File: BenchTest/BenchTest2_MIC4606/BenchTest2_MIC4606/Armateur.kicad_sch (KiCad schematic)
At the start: 15 parts, among them Q1 Q_NMOS_DGS, Q2 Q_NMOS_DGS, U1 TLP2767

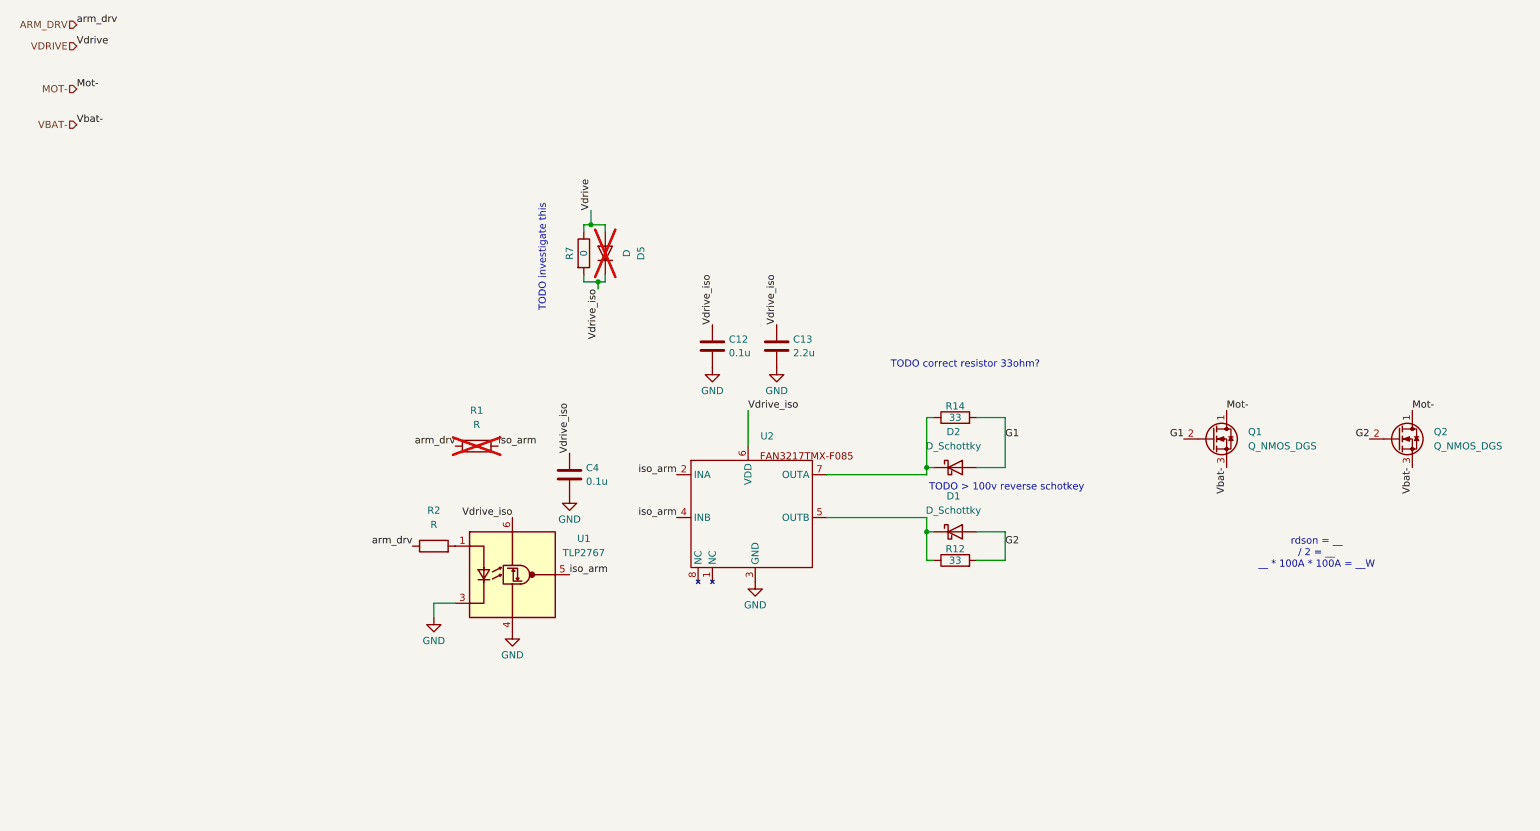
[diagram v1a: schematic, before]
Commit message: Defined Some parts, added notes for Arm/regen/H bridge
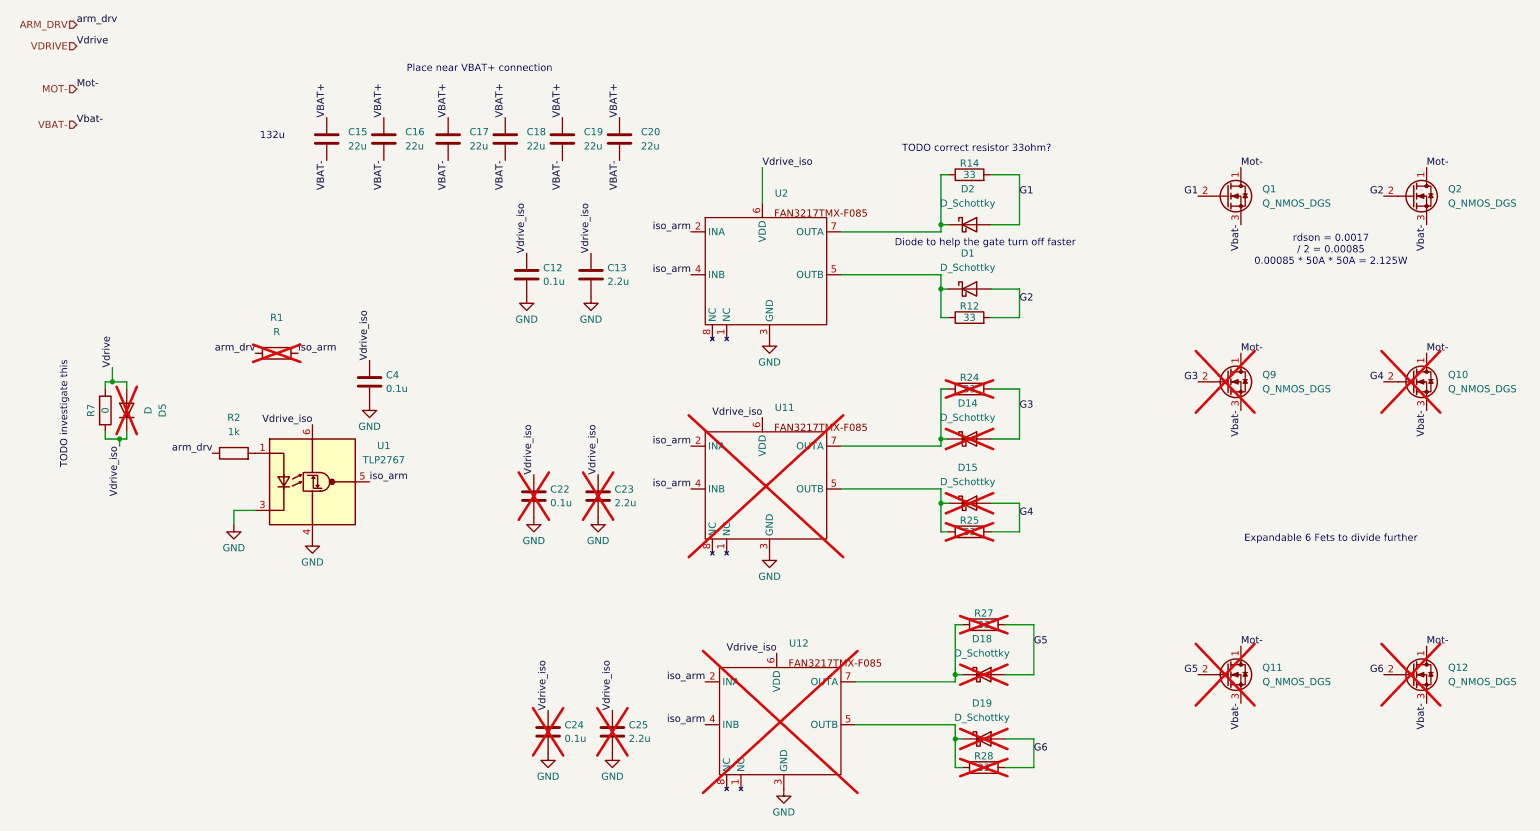
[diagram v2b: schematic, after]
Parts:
- added C15, C16, C17, C18, C19, C20: 22u, symbol Device:C
- added C22, C24: 0.1u, Capacitor_SMD:C_0402_1005Metric_Pad0.74x0.62mm_HandSolder, symbol Device:C
- added C23, C25: 2.2u, Capacitor_SMD:C_0603_1608Metric_Pad1.08x0.95mm_HandSolder, symbol Device:C
- added D14, D15, D18, D19: D_Schottky, symbol Device:D_Schottky
- added Q10, Q11, Q12, Q9: Q_NMOS_DGS, symbol Transistor_FET:Q_NMOS_DGS
- added R24, R25, R27, R28: 33, Resistor_SMD:R_0402_1005Metric_Pad0.72x0.64mm_HandSolder, symbol Device:R
- added U11, U12: ~, Package_SO:SOIC-8_3.9x4.9mm_P1.27mm, symbol New_Library:FAN3217
- R2: value R -> 1k
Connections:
- net GND: now also C22.2, C23.2, C24.2, C25.2, U11.3 (GND), U12.3 (GND)
- net MOT-: now also Q10.1 (D), Q11.1 (D), Q12.1 (D), Q9.1 (D)
- net VBAT-: now also C15.2, C16.2, C17.2, C18.2, C19.2, C20.2, Q10.3 (S), Q11.3 (S), Q12.3 (S), Q9.3 (S)
- net Vdrive_iso: now also C22.1, C23.1, C24.1, C25.1, U11.6 (VDD), U12.6 (VDD)
- net iso_arm: now also U11.2 (INA), U11.4 (INB), U12.2 (INA), U12.4 (INB)
- new net: D18.1 (K), R27.1, U12.7 (OUTA)
- new net: D19.1 (K), R28.1, U12.5 (OUTB)
- new net: D15.1 (K), R25.1, U11.5 (OUTB)
- new net: D14.1 (K), R24.1, U11.7 (OUTA)
- new net G3: D14.2 (A), Q9.2 (G), R24.2
- new net G4: D15.2 (A), Q10.2 (G), R25.2
- new net G5: D18.2 (A), Q11.2 (G), R27.2
- new net G6: D19.2 (A), Q12.2 (G), R28.2
- new net VBAT+: C15.1, C16.1, C17.1, C18.1, C19.1, C20.1
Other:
- note added: "132u"
- note added: "Diode to help the gate turn off faster"
- note added: "Expandable 6 Fets to divide further"
- note added: "Place near VBAT+ connection"
- note added: "rdson = 0.0017 / 2 = 0.00085 0.00085 * 50A * 50A = 2.125W"
- note removed: "TODO > 100v reverse schotkey"
- note removed: "rdson = __ / 2 = __ __ * 100A * 100A = __W"
- moved on the sheet: C12, C13, C4, D1, D2, D5, Q1, Q2, R1, R12, R14, R2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

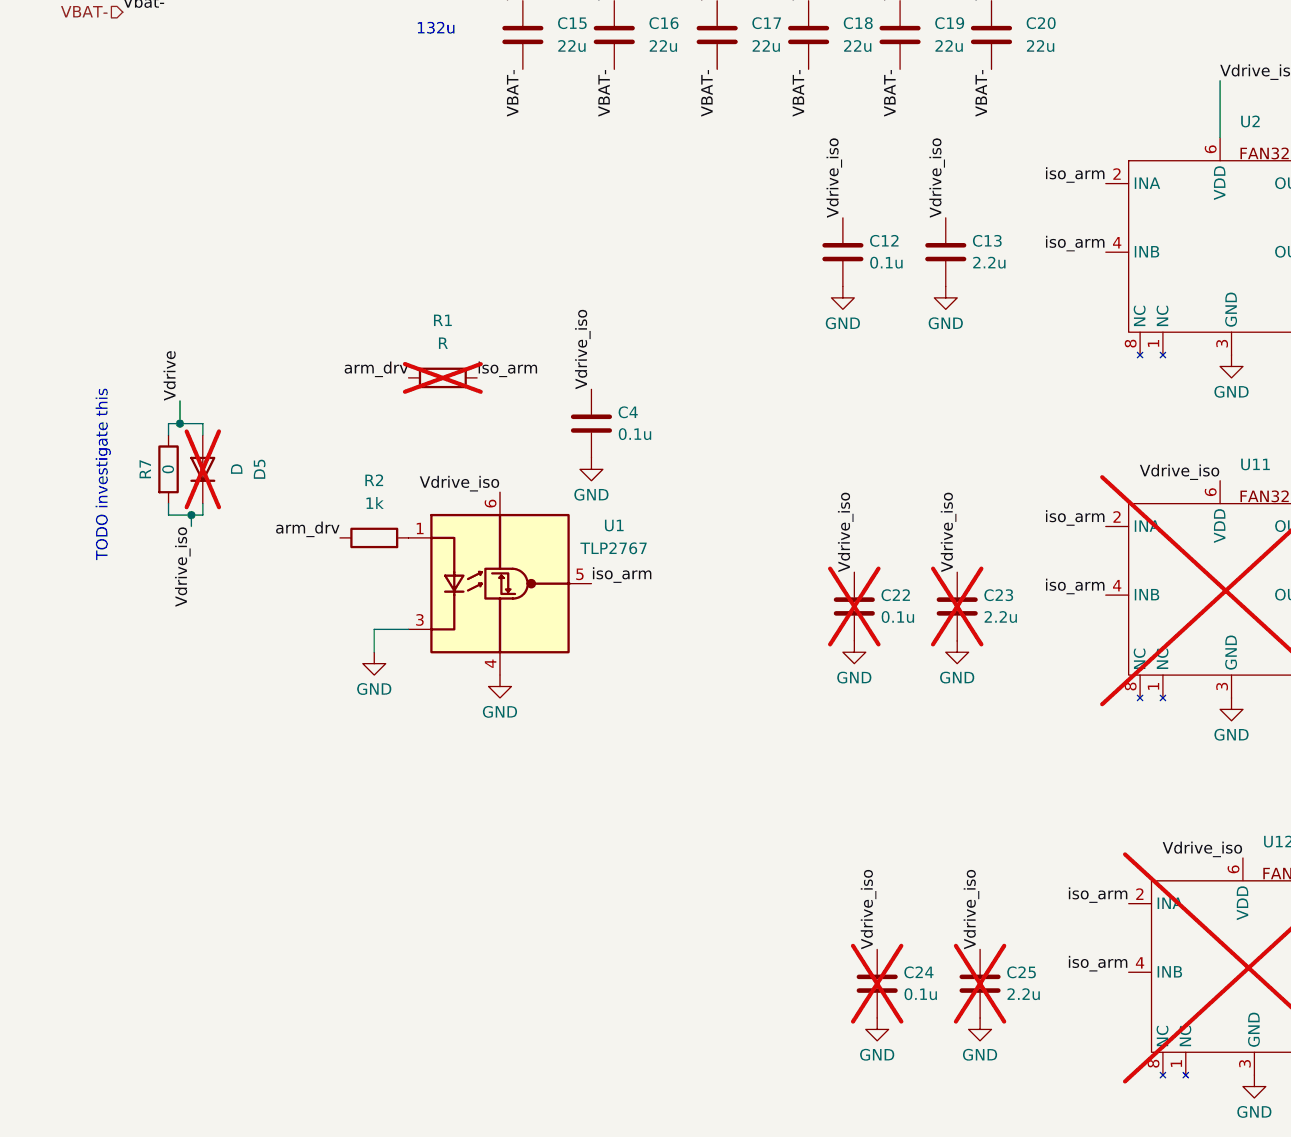
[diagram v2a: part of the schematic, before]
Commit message: Removed Optoisolators from digital Signals
Will be requiring these on the drive side
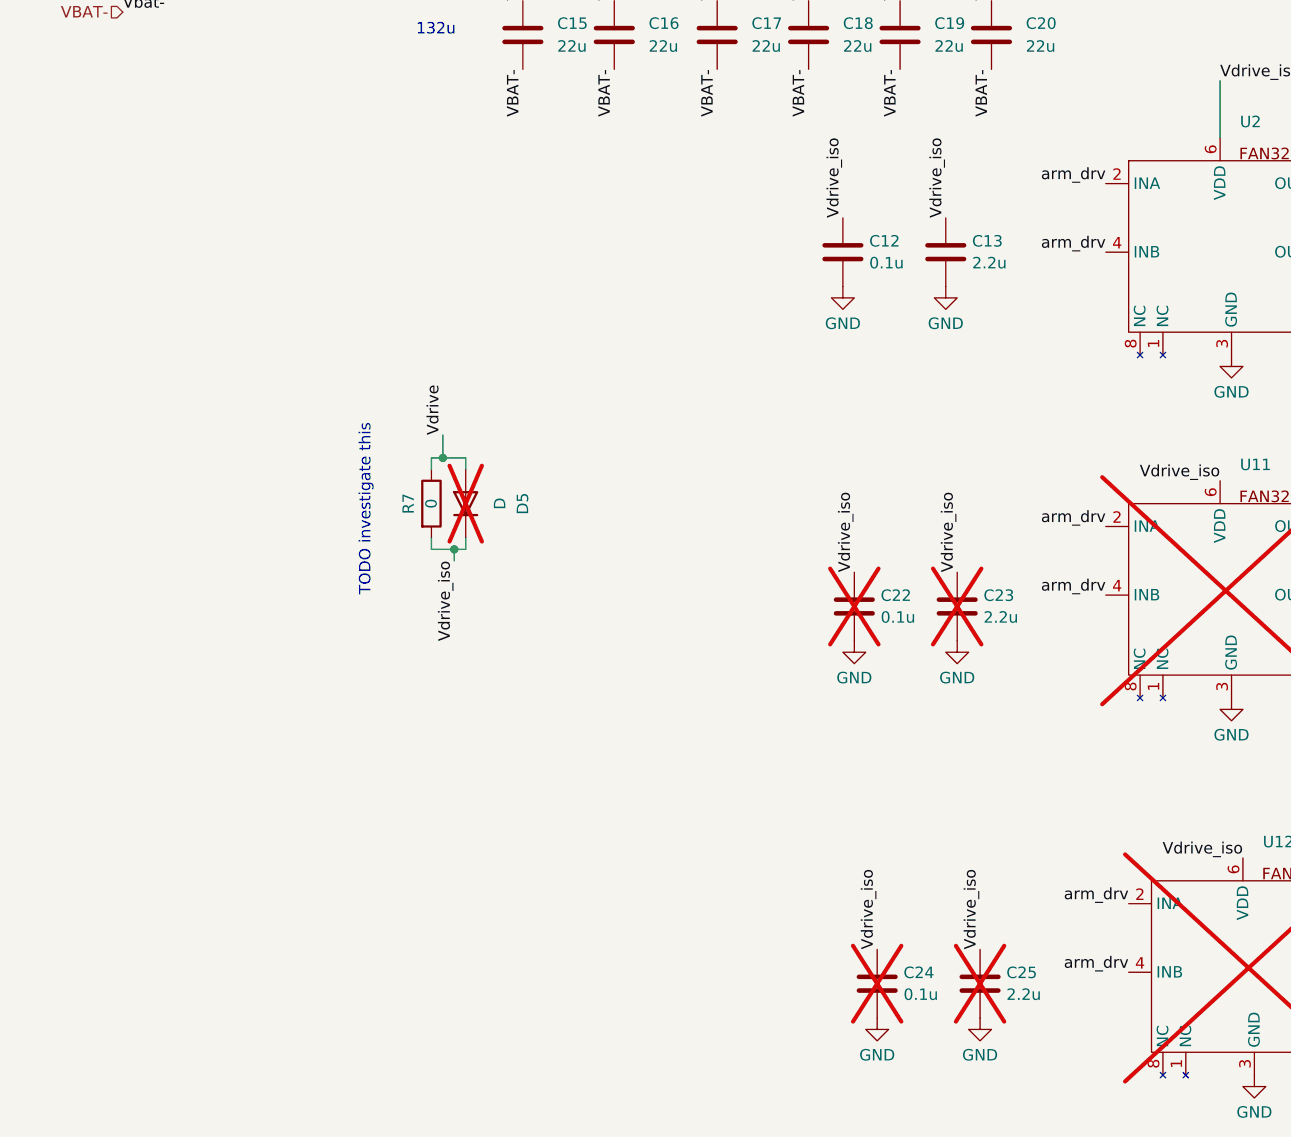
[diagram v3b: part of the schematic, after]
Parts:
- removed C4: 0.1u, Capacitor_SMD:C_0402_1005Metric_Pad0.74x0.62mm_HandSolder, symbol Device:C
- removed R1: R, symbol Device:R
- removed R2: 1k, symbol Device:R
- removed U1: TLP2767, Package_SO:SO-6L_10x3.84mm_P1.27mm, symbol Isolator:TLP2767
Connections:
- net iso_arm is gone; now on net ARM_DRV: U11.2 (INA), U11.4 (INB), U12.2 (INA), U12.4 (INB), U2.2 (INA), U2.4 (INB)
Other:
- moved on the sheet: D5, R7

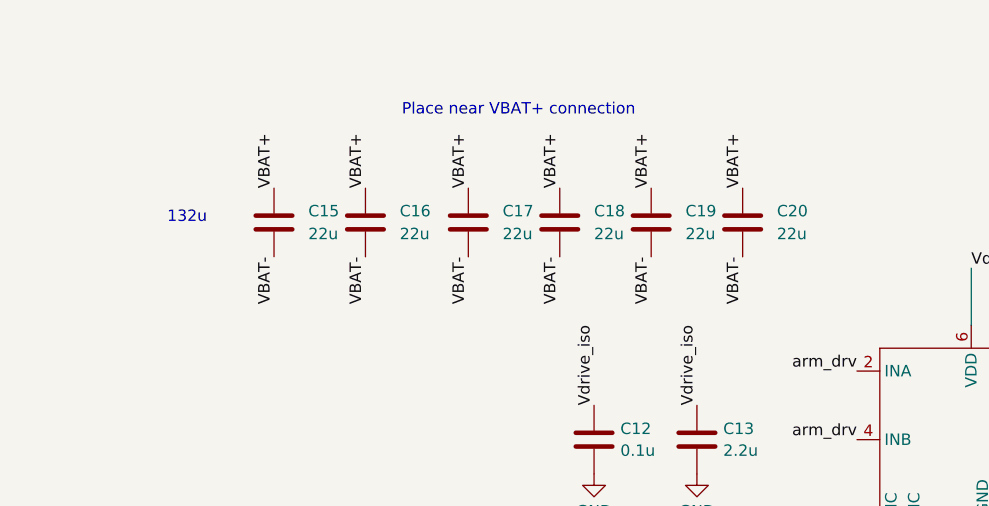
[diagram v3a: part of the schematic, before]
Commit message: Footprint / Capacitor Assignment
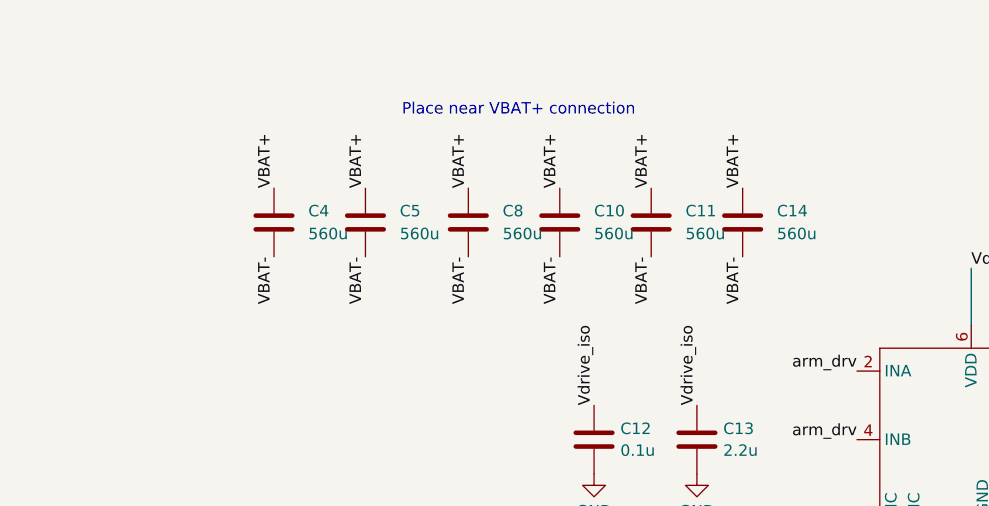
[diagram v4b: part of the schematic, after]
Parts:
- removed C15, C16, C17, C18, C19, C20: 22u, symbol Device:C
- added C10, C11, C14, C4, C5, C8: 560u, Capacitor_THT:C_Radial_D18.0mm_H35.5mm_P7.50mm, symbol Device:C
- D1, D14, D15, D18, D19, D2, D5: footprint (none) -> Diode_SMD:D_0603_1608Metric_Pad1.05x0.95mm_HandSolder
- R7: footprint (none) -> Resistor_SMD:R_0402_1005Metric_Pad0.72x0.64mm_HandSolder
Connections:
- net VBAT+: now also C10.1, C11.1, C14.1, C4.1, C5.1, C8.1
- net VBAT-: now also C10.2, C11.2, C14.2, C4.2, C5.2, C8.2
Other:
- note removed: "132u"
